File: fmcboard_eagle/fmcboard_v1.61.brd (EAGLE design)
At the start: 147 x 74 mm, 208 parts, among them IC1 OPA699ID, IC10 LM358, IC11 7805TV, IC12 SN74AUC2G66DCTR, IC13 SN74AUC2G66DCTR, IC14 SN74AUC2G66DCTR, IC15 SN74AUC2G66DCTR, IC16 DAC7578SPWR, IC17 SN74AUC2G66DCTR, IC18 SN74AUC2G66DCTR, IC19 SN74AUC2G66DCTR, IC2 DAC7578SPWR, IC20 SN74AUC2G66DCTR, IC21 74AUP2GU04GW, IC22 74AUP2GU04GW, IC23 74AUP2GU04GW, IC24 74AUP2GU04GW, IC25 LM358, IC26 AMS1117-1.8, IC3 LTC6229IMS8E#TRPBF, IC4 LTC6229IMS8E#TRPBF, IC5 LTC6229IMS8E#TRPBF, IC6 OPA699ID, IC7 OPA699ID, IC8 LM358, IC9 LM358, J1 8pin, J10 8pin, J11 8pin, J12 4p-2.54, J2 ASP-134604-01, J3 4p-2.54, J4 4p-2.54, J5 8pin, J6 4p-2.54, J7 4p-2.54, J8 4p-2.54, J9 8pin, U1 TXS0108EPWR, U2 STMICROELECTRONICS_L7905ACVST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

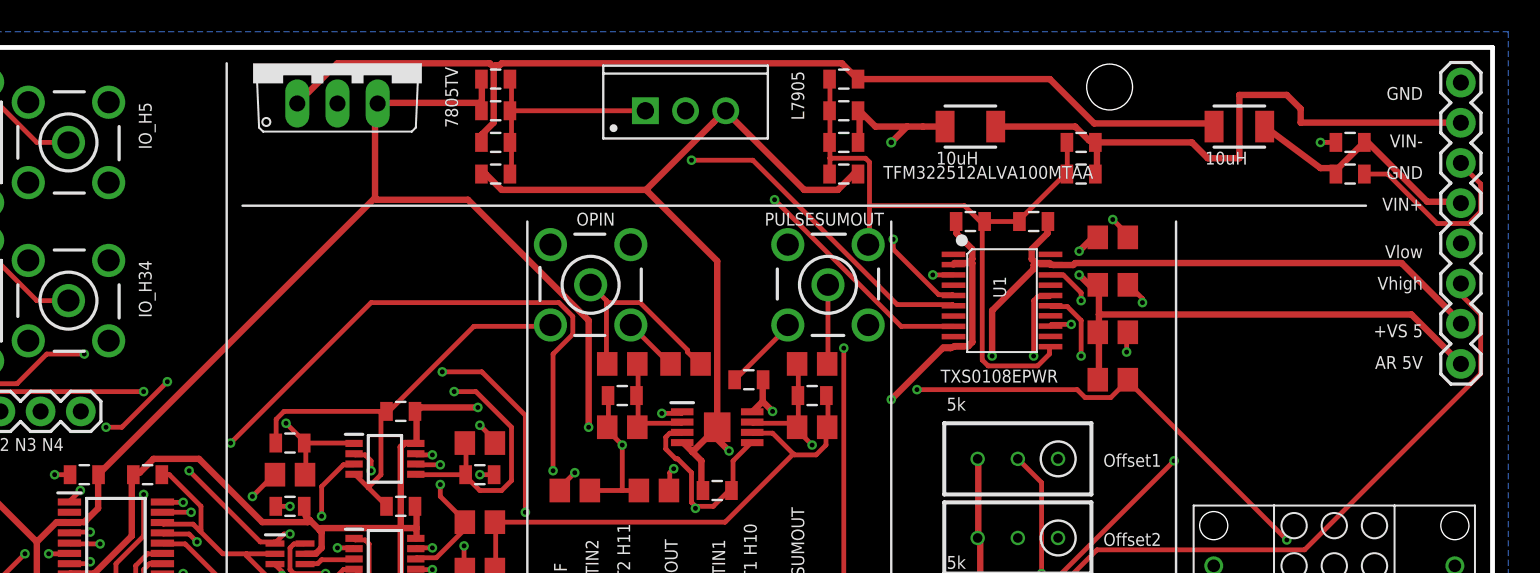
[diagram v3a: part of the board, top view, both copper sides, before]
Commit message: route power better
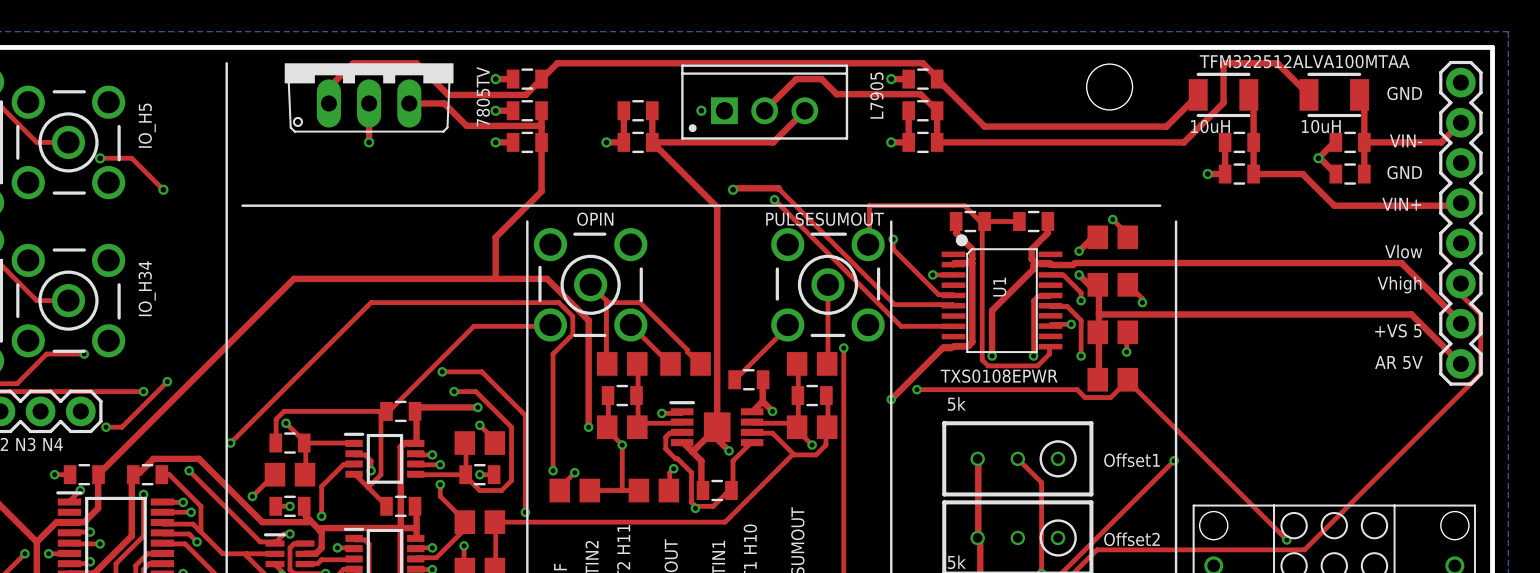
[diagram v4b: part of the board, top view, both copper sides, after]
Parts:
- moved L2 23.1 mm to (137.0, 71.0)
- moved C41 17.0 mm to (138.0, 66.0)
- moved C44 17.0 mm to (138.0, 68.0)
- moved C39 13.2 mm to (93.0, 68.0)
- moved C76 9.85 mm to (93.0, 70.0), turned to 180 degrees
- moved C1 7.00 mm to (131.0, 66.0), turned to 180 degrees
- moved C42 7.00 mm to (131.0, 68.0)
- moved C40 5.00 mm to (111.0, 68.0)
- moved C43 5.00 mm to (111.0, 72.0)
- moved C45 5.00 mm to (111.0, 70.0)
- moved U2 5.00 mm to (101.0, 70.0)
- moved C2 4.47 mm to (86.0, 72.0), turned to 180 degrees
- moved C38 2.83 mm to (86.0, 68.0), turned to 180 degrees
- moved C47 2.83 mm to (86.0, 70.0), turned to 180 degrees
- moved L1 2.24 mm to (130.0, 71.0)
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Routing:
- net GND: track 451.6 -> 424.6 mm, vias 43 -> 52
- net VIN-: track 37.7 -> 11.7 mm
- net VIN-CLEAN: track 23.3 -> 42.4 mm, vias 1 -> 0
- net VS-: track 305.3 -> 291.8 mm
- net VIN+CLEAN: track 65.9 -> 61.2 mm
- net VIN+: track 16.3 -> 19.1 mm
- net VS+: track 330.0 -> 331.4 mm
- net G37: track 110.3 -> 110.6 mm, vias 2 -> 4

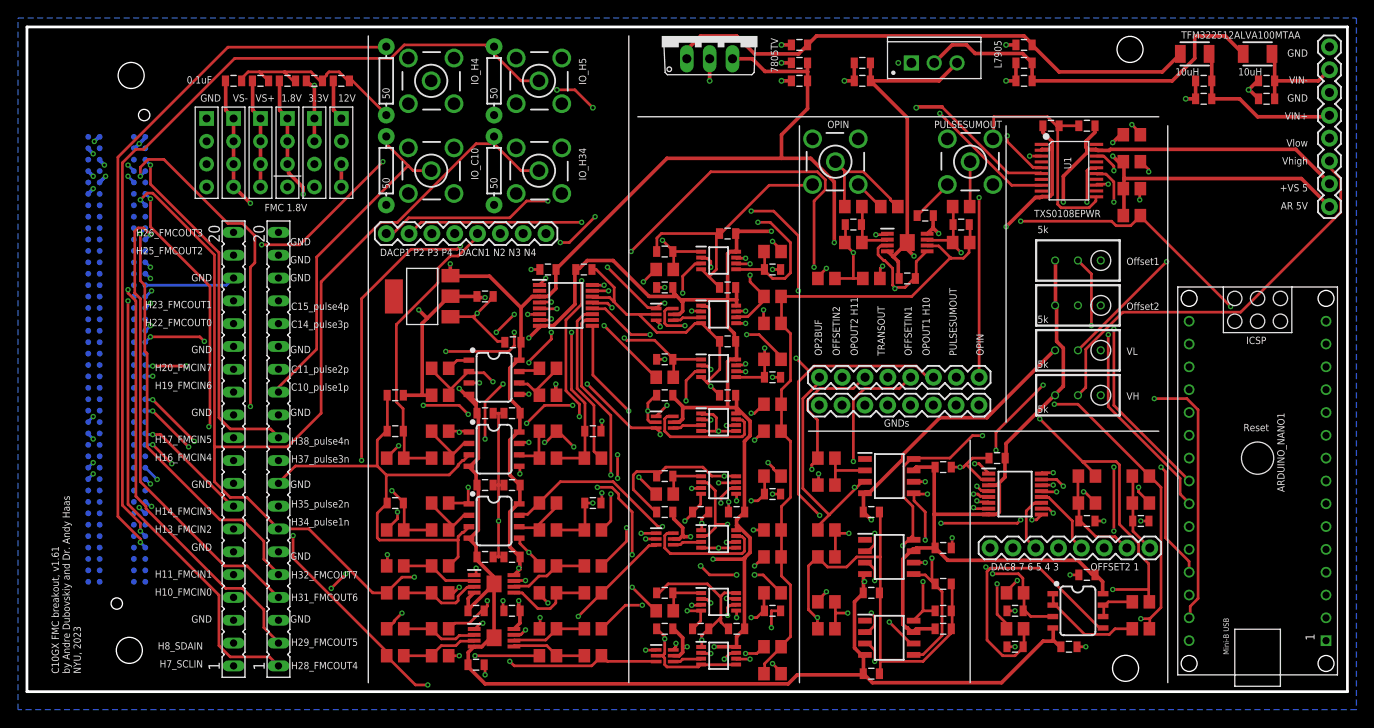
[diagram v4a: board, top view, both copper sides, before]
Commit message: v1.61: Fix 1v8- 1k->330 fo 16 100->330 for 9 1pF and 10k pulldown on opin 10k pulldowns on neg pulse inputs
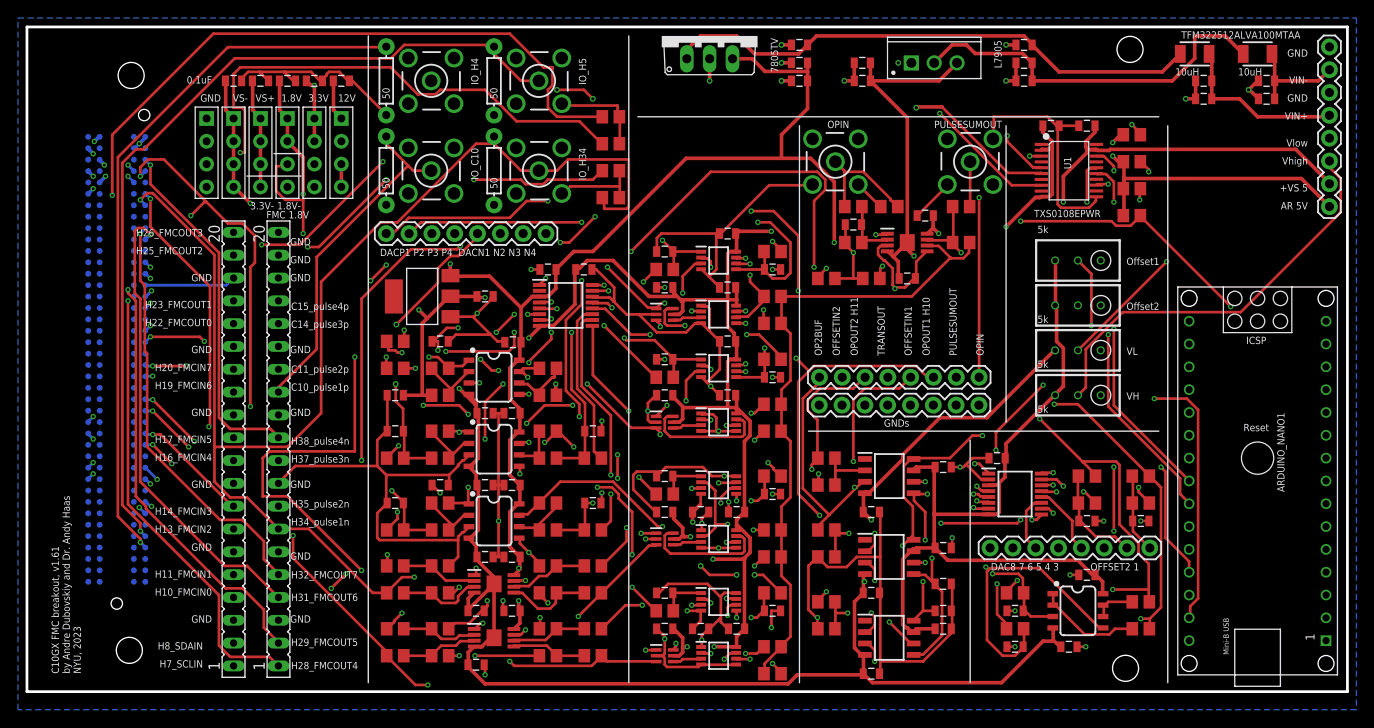
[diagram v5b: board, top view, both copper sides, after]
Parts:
- added C77: 1uF, SparkFun-Passives:0805
- added R78, R79: 100, rcl:R0805
- added R80, R81, R82, R83: 10k, rcl:R0805
- C32: value 1pF? -> 1uF
- C33: value 1pF? -> 1pF
- R1, R12, R32, R33, R36, R38, R40, R7, R8: value 100 -> 330
- R21, R22, R23, R24, R27, R28, R29, R30, R37, R39, R41, R43, R44, R45, R46, R52: value 1k -> 330
- R42: value 50? -> 1k
- moved C32 59.4 mm to (46.0, 39.0)
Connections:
- new net $N99: IC10.2, R71.1, R72.1
- new net N$37: IC10.6, R70.1, R73.1
- net 1V8: no longer J12.3
- net 1V8-: now also C77.2, J12.3, R78.1; no longer IC10.2, R71.1, R72.1
- net 3V3: no longer J3.4
- net 3V3-: now also C32.2, J3.4, R79.1; no longer IC10.6, R70.1, R73.1
- net GND: now also C32.1, C77.1, R80.2, R81.2, R82.2, R83.2
- net H34: now also R80.1
- net H35: now also R81.1
- net H37: now also R83.1
- net H38: now also R82.1
- net N$35: now also IC10.1, R71.2, R78.2; no longer IC10.7, R70.2
- net N$36: now also IC10.7, R70.2, R79.2; no longer IC10.1, R71.2
- net PULSESUMIN: no longer C32.1
- net PULSESUMOUT: no longer C32.2
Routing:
- net H37: track 104.7 -> 189.9 mm, vias 5 -> 7
- net H38: track 98.0 -> 164.3 mm, vias 2 -> 3
- net H35: track 99.3 -> 156.3 mm, vias 3 -> 6
- net 1V8-: track 144.2 -> 193.3 mm, vias 7 -> 11
- net N$36: track 2.62 -> 35.3 mm, vias 0 -> 6
- net 3V3-: track 6.99 -> 35.0 mm, vias 0 -> 3
- net GND: track 424.6 -> 451.5 mm
- net H34: track 156.1 -> 176.1 mm
- net N$37: track 0.00 -> 7.15 mm
- net $N99: track 0.00 -> 6.87 mm
- net N$35: track 2.42 -> 8.70 mm, vias 0 -> 2
- net C15: track 87.5 -> 91.7 mm
- net PULSESUMIN: track 75.2 -> 73.1 mm
- net DACN1: track 32.8 -> 32.9 mm, vias 0 -> 2
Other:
- board text added: "1.8V-"
- board text added: "3.3V-"

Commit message: v1.61: Add OPA695 for transimpedance and first stage of opin amp
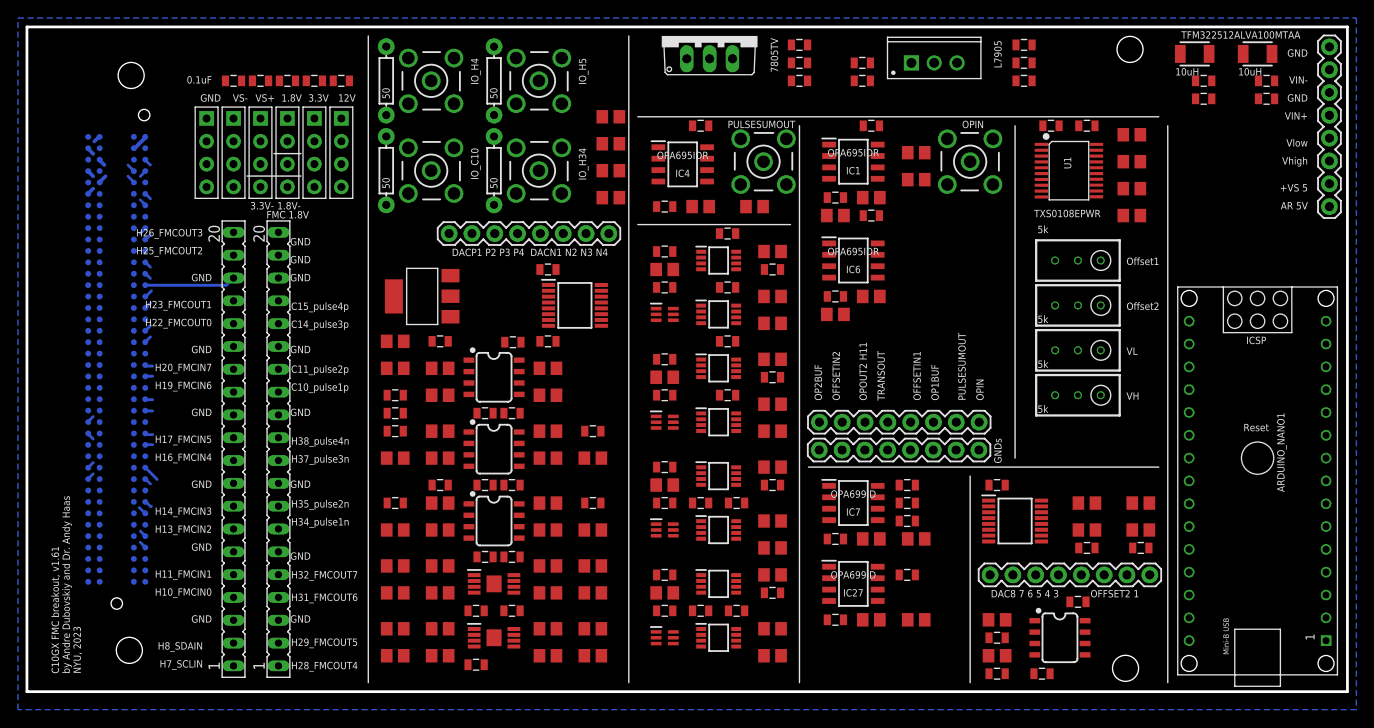
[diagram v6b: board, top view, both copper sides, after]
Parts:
- removed C33: 1pF, SparkFun-Passives:0805
- removed R13: 1k, rcl:R0805
- removed R14, R35: 4.7k, rcl:R0805
- added C78, C79: 0.1uF, SparkFun-Passives:0805
- added IC27: OPA699ID, OPA699ID:SOIC127P600X175-8N
- IC1, IC6: value OPA699ID -> OPA695IDR; device OPA699ID:SOIC127P600X175-8N -> OPA695IDR:SOIC127P600X175-8N
- IC4: value LTC6229IMS8E#TRPBF -> OPA695IDR; device LTC6229IMS8E#TRPBF:SOP65P490X110-9N -> OPA695IDR:SOIC127P600X175-8N
- R11, R6, R9: value 1k -> 470
- R18: value 1k -> 330
- R19: value 100 -> 47
- R42: value 1k -> 10k
- moved IC1 53.2 mm to (92.0, 59.0)
- moved IC6 33.2 mm to (92.0, 48.0)
- moved R1 29.3 mm to (75.0, 54.0), turned to 0 degrees
- moved C26 29.1 mm to (94.0, 53.0), turned to 180 degrees
- moved C46 28.2 mm to (71.0, 54.0)
- moved R19 27.0 mm to (90.0, 42.0)
- moved C16 26.9 mm to (75.0, 63.0)
- moved R18 26.5 mm to (94.0, 44.0), turned to 0 degrees
- moved IC4 26.5 mm to (73.0, 58.7)
- moved C27 24.3 mm to (90.0, 44.0)
- moved PULSESUMOUT 23.0 mm to (82.0, 59.0)
- moved R34 23.0 mm to (81.0, 54.0)
- moved C34 16.4 mm to (41.0, 31.0), turned to 180 degrees
- moved OPIN 15.0 mm to (105.0, 59.0)
- moved C7 14.6 mm to (98.0, 23.0)
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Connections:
- removed net N$3: IC1.2, R10.2, R9.1
- new net OP1BUF: IC6.6, IC7.3, J5.3, R18.2
- net DACOFFSET1: no longer R35.2
- net GND: now also C78.2, C79.2, IC1.3; no longer IC4.5
- net N$1: now also IC27.2, R10.2, R9.1; no longer IC1.3, R13.1, R14.1, R35.1
- net OFFSETOUT1: no longer R14.2
- net OP2BUF: now also IC27.3, IC7.6, R6.2; no longer IC6.6, IC7.3, R18.2
- net OPOUT1_H10: no longer IC1.6, J5.3, R9.2
- net OPOUT2_H11: now also IC27.6, R9.2; no longer IC7.6, R6.2
- net PULSESUMIN: now also IC4.2; no longer IC4.6
- net PULSESUMOUT: now also IC4.6; no longer IC4.7
- net TRANSIN: now also IC1.2; no longer C33.1, IC4.2
- net TRANSOUT: now also IC1.6; no longer C33.2, IC4.1, R13.2
- net VH: now also IC27.8; no longer IC1.8, IC6.8
- net VL: now also IC27.5; no longer IC1.5, IC6.5
- net VS+: now also C78.1, IC27.7, IC4.7; no longer IC4.8
- net VS-: now also C79.1, IC27.4; no longer IC4.9
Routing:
- net GND: track 451.5 -> 10.3 mm, vias 52 -> 0
- net VS+: track 331.5 -> 0.00 mm, vias 6 -> 0
- net VS-: track 291.8 -> 0.00 mm, vias 5 -> 0
- net 1V8: track 229.1 -> 0.00 mm, vias 10 -> 0
- net 1V8-: track 193.3 -> 0.00 mm, vias 11 -> 0
- net H37: track 189.9 -> 0.80 mm, vias 7 -> 0
- net SCLIN: track 186.5 -> 0.94 mm, vias 2 -> 0
- net H34: track 176.1 -> 0.82 mm, vias 3 -> 0
- net H38: track 164.3 -> 0.83 mm, vias 3 -> 0
- net SDAIN: track 160.5 -> 0.91 mm, vias 4 -> 0
- net H35: track 156.3 -> 0.79 mm, vias 6 -> 0
- net OPOUT1_H10: track 151.4 -> 0.79 mm, vias 9 -> 0
- net OPOUT2_H11: track 140.5 -> 1.86 mm, vias 3 -> 0
- net AR_SDAIN2: track 136.9 -> 0.00 mm, vias 4 -> 0
- net AR_SCLIN2: track 133.5 -> 0.00 mm, vias 3 -> 0
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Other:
- board text added: "OP1BUF"
- board text removed: "OPOUT1 H10"

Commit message: routed
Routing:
- net GND: track 10.3 -> 520.5 mm, vias 0 -> 41
- net VS+: track 0.00 -> 330.6 mm, vias 0 -> 12
- net VS-: track 0.00 -> 319.3 mm, vias 0 -> 2
- net 1V8: track 0.00 -> 238.0 mm, vias 0 -> 10
- net SDAIN: track 0.91 -> 225.6 mm, vias 0 -> 2
- net SCLIN: track 0.94 -> 193.2 mm, vias 0 -> 4
- net AR_SCLIN2: track 0.00 -> 162.7 mm, vias 0 -> 5
- net H38: track 0.83 -> 157.3 mm, vias 0 -> 4
- net H37: track 0.80 -> 155.6 mm, vias 0 -> 5
- net H35: track 0.79 -> 149.4 mm, vias 0 -> 6
- net H34: track 0.82 -> 147.6 mm, vias 0 -> 4
- net 1V8-: track 0.00 -> 139.8 mm, vias 0 -> 7
- net AR_SDAIN2: track 0.00 -> 134.8 mm, vias 0 -> 5
- net OPOUT2_H11: track 1.86 -> 130.4 mm, vias 0 -> 4
- net C10: track 0.81 -> 128.3 mm, vias 0 -> 5
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
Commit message: routed
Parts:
- removed C11: 0.1uF, SparkFun-Passives:0805
- removed C32, C65: 1uF, SparkFun-Passives:0805
- removed IC25: LM358, SparkFun-IC-Amplifiers:SO08
- removed J10, J11: 8pin, SparkFun-Connectors:1X08
- removed R3: 100k, rcl:R0805
- removed R61, R79: 100, rcl:R0805
- removed R70, R73: 1k, rcl:R0805
- removed R_O1: 5k, resistor:RTRIM3296W
- moved C75 78.0 mm to (45.0, 40.0), turned to 0 degrees
- moved C25 72.0 mm to (96.0, 72.0), turned to 180 degrees
- moved R25 66.7 mm to (59.0, 36.0), turned to 180 degrees
- moved C9 63.7 mm to (49.0, 47.0)
- moved IC16 63.7 mm to (51.0, 43.0)
- moved C64 62.8 mm to (63.0, 31.0)
- moved R60 62.8 mm to (63.0, 33.0)
- moved R31 57.0 mm to (63.0, 36.0)
- moved C4 56.9 mm to (59.0, 31.0), turned to 0 degrees
- moved R17 56.9 mm to (59.0, 33.0), turned to 0 degrees
- moved C28 28.8 mm to (108.0, 48.0)
- moved C7 28.8 mm to (108.0, 50.0)
- moved C8 28.8 mm to (108.0, 46.0)
- moved IC7 28.8 mm to (102.0, 48.0)
- moved R6 28.8 mm to (104.0, 44.0), turned to 0 degrees
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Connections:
- net OPOUT1_H10 renamed H10
- removed net 3V3-: C32.2, J3.4, R79.1
- removed net DAC3: IC16.5, J10.3
- removed net DAC4: IC16.12, J10.4
- removed net DAC5: IC16.6, J10.5
- removed net DAC6: IC16.11, J10.6
- removed net DAC7: IC16.7, J10.7
- removed net DAC8: IC16.10, J10.8
- removed net DACOFFSET1: C64.2, J10.1, R60.2
- removed net DACOFFSET2: C65.1, J10.2, R31.2, R61.1
- removed net N$30: IC16.13, R61.2
- removed net N$36: IC10.7, R70.2, R79.2
- removed net N$37: IC10.6, R70.1, R73.1
- removed net N$8: R3.2, R_O1.2
- removed net OFFSETIN1: C11.1, IC25.3, J5.4, R3.1
- removed net OFFSETIN2: C4.1, IC25.5, J5.7, R17.1
- removed net OFFSETOUT1: IC25.1, IC25.2
- removed net OFFSETOUT2: IC25.6, IC25.7, R25.2
- removed net OPOUT2_H11: IC27.6, J2.H11, J5.6, R9.2, SV1.5
- new net DACOFFSET: C64.2, J5.6, R31.2, R60.2
- new net OFFSETIN: C4.1, IC10.5, R17.1
- new net OFFSETOUT: IC10.6, IC10.7, J5.5, R25.2
- new net OPOUT_H11: IC27.6, J2.H11, J5.8, R9.2, SV1.5
- net 3V3: now also J3.4; no longer R73.2
- net GND: now also J5.1, J5.3, J5.7; no longer C11.2, C32.1, C65.2, IC10.5, J11.1, J11.2, J11.3, J11.4, J11.5, J11.6, J11.7, J11.8
- net IO1: no longer J5.1
- net OP1BUF: no longer J5.3
- net OP2BUF: no longer J5.8
- net TRANSOUT: now also J5.4; no longer J5.5
- net VS+: no longer IC25.8, R_O1.3
- net VS-: no longer IC25.4, R_O1.1
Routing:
- net OPOUT_H11: track 0.00 -> 134.8 mm, vias 0 -> 2
- net OPOUT2_H11: track 130.4 -> 0.00 mm, vias 4 -> 0
- net DACLDAC: track 98.3 -> 12.6 mm, vias 4 -> 2
- net DACCLR: track 102.6 -> 20.8 mm, vias 6 -> 3
- net C15: track 90.5 -> 166.2 mm, vias 5 -> 4
- net N$2: track 44.1 -> 115.4 mm, vias 0 -> 7
- net VS-: track 319.3 -> 259.7 mm, vias 2 -> 4
- net OFFSETIN2: track 53.4 -> 0.00 mm, vias 1 -> 0
- net OFFSETOUT: track 0.00 -> 51.4 mm, vias 0 -> 4
- net SDAIN: track 225.6 -> 174.6 mm, vias 2 -> 3
- net AR_SCLIN2: track 162.7 -> 117.4 mm, vias 5 -> 6
- net N$8: track 44.9 -> 0.00 mm
- net DACOFFSET: track 0.00 -> 43.4 mm, vias 0 -> 3
- net OFFSETIN1: track 34.1 -> 0.00 mm, vias 1 -> 0
- net 3V3: track 80.1 -> 46.5 mm, vias 3 -> 5
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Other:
- board text added: "DACOFFSET"
- board text added: "OFFSETOUT"
- board text added: "OPOUT_H11"
- board text added: "Offset"
- board text removed: "3.3V-"
- board text removed: "DAC8 7 6 5 4 3 OFFSET2 1"
- board text removed: "GNDs"
- board text removed: "OFFSETIN1"
- board text removed: "OFFSETIN2"
- board text removed: "OP1BUF"
- board text removed: "OP2BUF"
- board text removed: "OPIN"
- board text removed: "OPOUT2 H11"
- board text removed: "Offset1"
- board text removed: "Offset2"
